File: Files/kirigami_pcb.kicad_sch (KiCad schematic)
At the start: 15 parts, among them J1 In, J2 Thermistor, J3 Heater, J4 Fuse, J5 Fan, J6 Neopixel

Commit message: chain order
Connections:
- net DataIn: now also D8.2 (DOUT); no longer J1.4 (Pin_4)
- net DataOut: now also J1.3 (Pin_3); no longer D1.4 (DIN)
- new net: D1.4 (DIN), J1.4 (Pin_4)
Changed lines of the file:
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@@
     (stroke (width 0) (type default))
   )
-  (wire (pts (xy 73.66 76.2) (xy 73.66 92.71))
+  (wire (pts (xy 73.66 76.2) (xy 73.66 105.41))
     (stroke (width 0) (type default))
   )
   (wire (pts (xy 87.63 73.66) (xy 99.06 73.66))
-    (stroke (width 0) (type default))
-  )
-  (wire (pts (xy 73.66 92.71) (xy 111.76 92.71))
     (stroke (width 0) (type default))
   )
@@
     (stroke (width 0) (type default))
   )
+  (wire (pts (xy 73.66 105.41) (xy 77.47 105.41))
+    (stroke (width 0) (type default))
+  )
+  (wire (pts (xy 71.12 92.71) (xy 111.76 92.71))
+    (stroke (width 0) (type default))
+  )
   (wire (pts (xy 76.2 87.63) (xy 87.63 87.63))
     (stroke (width 0) (type default))
   )
   (wire (pts (xy 72.39 57.15) (xy 99.06 57.15))
+    (stroke (width 0) (type default))
+  )
+  (wire (pts (xy 111.76 95.25) (xy 72.39 95.25))
     (stroke (width 0) (type default))
   )
@@
     (stroke (width 0) (type default))
   )
-  (wire (pts (xy 77.47 95.25) (xy 111.76 95.25))
-    (stroke (width 0) (type default))
-  )
   (wire (pts (xy 130.81 113.03) (xy 146.05 113.03))
     (stroke (width 0) (type default))
@@
   )
   (wire (pts (xy 85.09 90.17) (xy 85.09 97.79))
+    (stroke (width 0) (type default))
+  )
+  (wire (pts (xy 72.39 95.25) (xy 72.39 73.66))
     (stroke (width 0) (type default))
   )
@@
     (stroke (width 0) (type default))
   )
-  (wire (pts (xy 77.47 95.25) (xy 77.47 105.41))
+  (wire (pts (xy 199.39 115.57) (xy 71.12 115.57))
     (stroke (width 0) (type default))
   )
@@
     (stroke (width 0) (type default))
   )
-  (wire (pts (xy 199.39 115.57) (xy 72.39 115.57))
+  (wire (pts (xy 71.12 115.57) (xy 71.12 92.71))
     (stroke (width 0) (type default))
   )
@@
     (stroke (width 0) (type default))
   )
-  (wire (pts (xy 72.39 115.57) (xy 72.39 73.66))
-    (stroke (width 0) (type default))
-  )

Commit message: round tracks
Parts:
- added C2, C3, C4, C5, C6, C7, C8, C9: Cap, Capacitor_SMD:C_0805_2012Metric_Pad1.18x1.45mm_HandSolder, symbol Device:C
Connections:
- net Neopixel5v: now also C1.2, D1.4 (DIN), J1.4 (Pin_4), C2.2, C3.2, C4.2, C5.2, C6.2, C7.2, C8.2, C9.2; no longer C1.1
- net NeopixelGND: now also C1.1, C2.1, C3.1, C4.1, C5.1, C6.1, C7.1, C8.1, C9.1; no longer C1.2
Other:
- moved on the sheet: C1

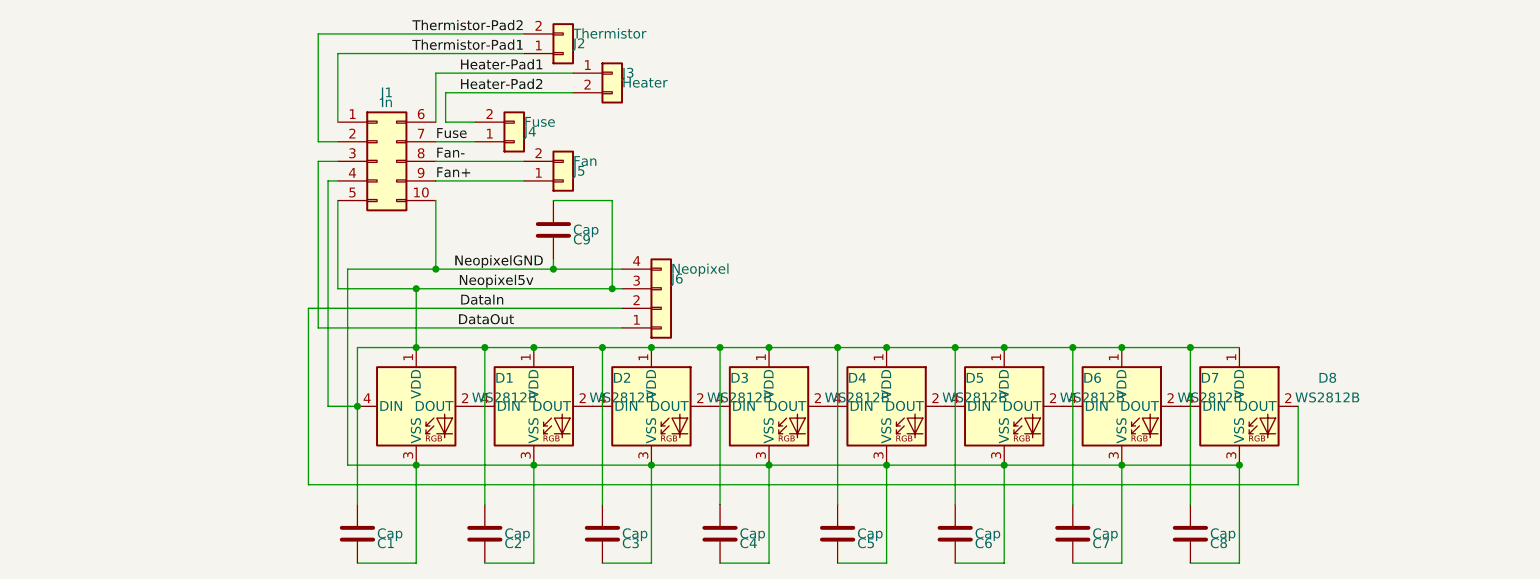
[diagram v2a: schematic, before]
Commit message: Schematic cleanup and organization
A few changes to the schematic to aid in readability as well as simplifying signal flow.
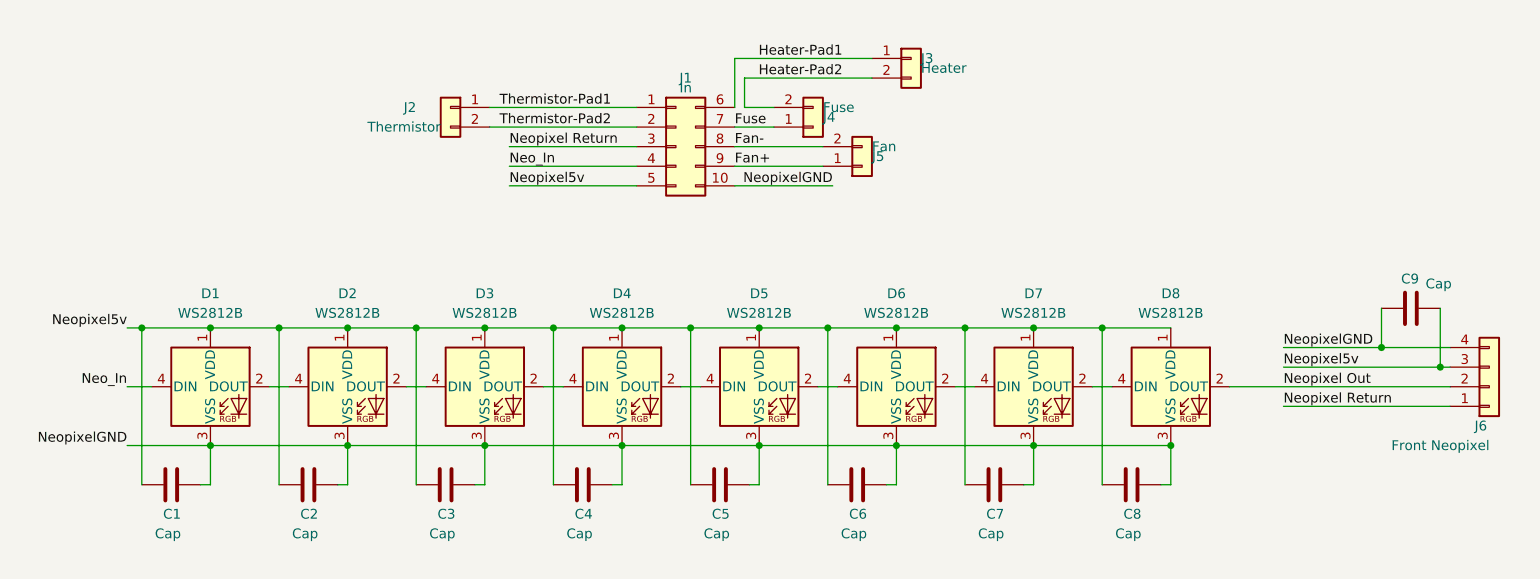
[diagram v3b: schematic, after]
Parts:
- J6: value Neopixel -> Front Neopixel
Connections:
- net Neopixel5v: now also C1.1, C2.1, C3.1, C4.1, C5.1, C6.1, C7.1, C8.1, C9.1; no longer C1.2, C2.2, C3.2, C4.2, C5.2, C6.2, C7.2, C8.2, C9.2, D1.4 (DIN), J1.4 (Pin_4)
- net NeopixelGND: now also C1.2, C2.2, C3.2, C4.2, C5.2, C6.2, C7.2, C8.2, C9.2; no longer C1.1, C2.1, C3.1, C4.1, C5.1, C6.1, C7.1, C8.1, C9.1
- net DataIn renamed Neopixel Out
- net DataOut renamed Neopixel Return
- new net Neo_In: D1.4 (DIN), J1.4 (Pin_4)
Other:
- moved on the sheet: C1, C3, C4, C5, C6, C7, C8, C9, D1, D2, D3, D4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
